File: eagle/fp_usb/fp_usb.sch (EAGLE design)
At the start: 6 parts, among them J3 USB-B-S-F-B-TH, J4 87583-3010RPALF, J5 TSM-105-01-S-SV

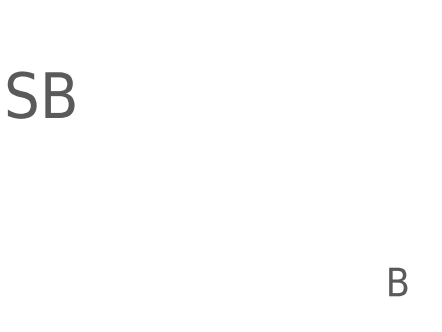
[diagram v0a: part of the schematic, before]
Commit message: Pre-production update.
* Increased clearances from chassis/enclosure ground.
* Improved text.
* Added gerbers.
* Added USB back panel.
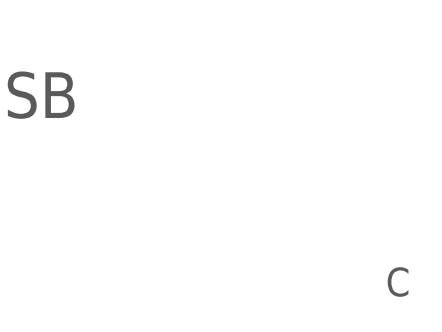
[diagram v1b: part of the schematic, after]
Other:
- note added: "C"
- note removed: "B"
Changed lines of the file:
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@@
 <?xml version="1.0" encoding="utf-8"?>
 <!DOCTYPE eagle SYSTEM "eagle.dtd">
-<eagle version="9.2.2">
+<eagle version="9.3.2">
 <drawing>
 <settings>
@@
 <plain>
 <text x="177.8" y="26.162" size="5.08" layer="97">Front Panel - USB</text>
-<text x="266.7" y="6.35" size="3.175" layer="97">B</text>
+<text x="266.7" y="6.35" size="3.175" layer="97">C</text>
 <text x="73.66" y="116.84" size="2.54" layer="97" align="center">IN</text>
 <text x="218.44" y="114.3" size="2.54" layer="97" align="center">OUT</text>

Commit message: Fixed eagle/fp_usb mounting hole location which was off by 0.18 mm (7 mil).
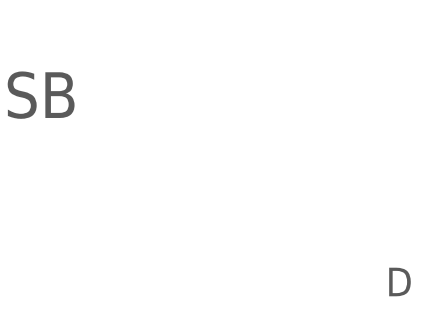
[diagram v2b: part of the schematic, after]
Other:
- note added: "D"
- note removed: "C"
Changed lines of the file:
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@@
 <?xml version="1.0" encoding="utf-8"?>
 <!DOCTYPE eagle SYSTEM "eagle.dtd">
-<eagle version="9.3.2">
+<eagle version="9.4.2">
 <drawing>
 <settings>
@@
 <plain>
 <text x="177.8" y="26.162" size="5.08" layer="97">Front Panel - USB</text>
-<text x="266.7" y="6.35" size="3.175" layer="97">C</text>
+<text x="266.7" y="6.35" size="3.175" layer="97">D</text>
 <text x="73.66" y="116.84" size="2.54" layer="97" align="center">IN</text>
 <text x="218.44" y="114.3" size="2.54" layer="97" align="center">OUT</text>
